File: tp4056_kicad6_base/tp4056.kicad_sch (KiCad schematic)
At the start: 32 parts, among them J1 USB_B_Micro, J10 Conn_01x02_Male, J2 Conn_01x01_Female, J3 Conn_01x01_Female, J4 Conn_01x01_Female, J5 Conn_01x01_Female, J6 Conn_01x01_Female, J7 Conn_01x01_Female, J8 Conn_01x02_Male, J9 Conn_01x02_Male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

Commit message: pcb. Board 38x18
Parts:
- J1: footprint usb_footprint:tp4056_USB_Micro-B_Molex_47346-0001_fix -> Connector_USB:USB_Micro-B_Molex-105017-0001
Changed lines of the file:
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@@
     (property "Reference" "J1" (id 0) (at 39.37 100.33 0))
     (property "Value" "USB_B_Micro" (id 1) (at 39.37 102.87 0))
-    (property "Footprint" "usb_footprint:tp4056_USB_Micro-B_Molex_47346-0001_fix" (id 2) (at 43.18 114.3 0)
+    (property "Footprint" "Connector_USB:USB_Micro-B_Molex-105017-0001" (id 2) (at 43.18 114.3 0)
       (effects (font (size 1.27 1.27)) hide)
     )
@@
     )
     (path "/ff08e3fa-c419-4101-acf6-7d150274f530"
-      (reference "J1") (unit 1) (value "USB_B_Micro") (footprint "usb_footprint:tp4056_USB_Micro-B_Molex_47346-0001_fix")
+      (reference "J1") (unit 1) (value "USB_B_Micro") (footprint "Connector_USB:USB_Micro-B_Molex-105017-0001")
     )
     (path "/f5af9e6d-b38e-432e-8453-2d6df2b3d8c9"

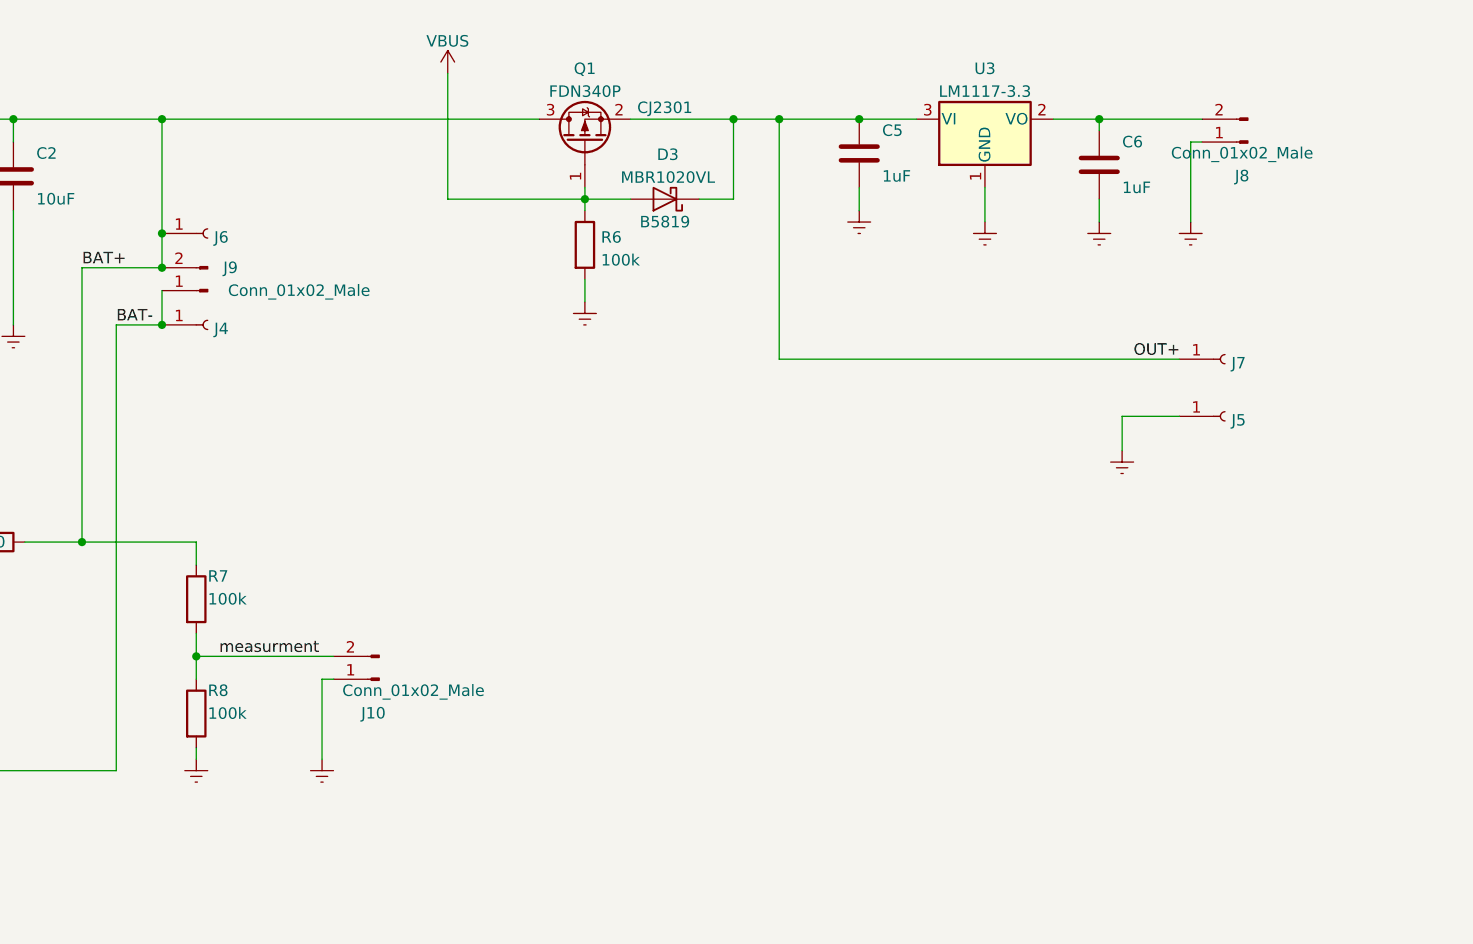
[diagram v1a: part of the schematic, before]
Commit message: sch. add voltage supervisor.
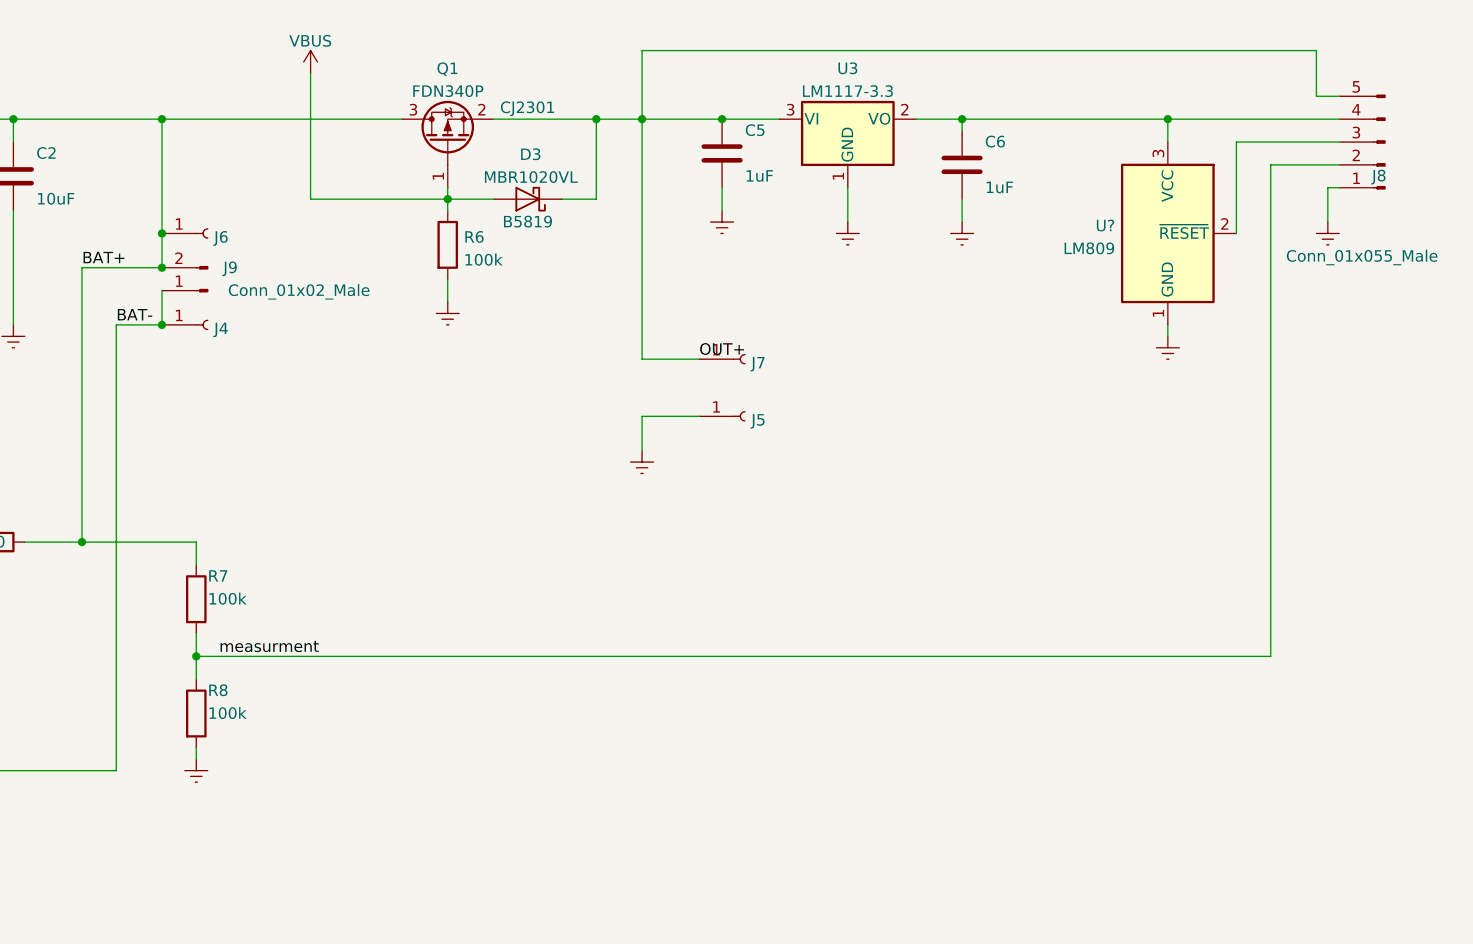
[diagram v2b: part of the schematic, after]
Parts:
- removed J10: Conn_01x02_Male, Connector_PinHeader_2.54mm:PinHeader_1x02_P2.54mm_Vertical, symbol Connector:Conn_01x02_Male
- added U?: LM809, Package_TO_SOT_SMD:SOT-23, symbol Power_Supervisor:LM809
- J8: value Conn_01x02_Male -> Conn_01x055_Male; footprint Connector_PinHeader_2.54mm:PinHeader_1x02_P2.54mm_Vertical -> Connector_PinHeader_2.54mm:PinHeader_1x04_P2.54mm_Vertical; symbol Connector:Conn_01x02_Male -> Connector:Conn_01x05_Male
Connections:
- net Earth: now also U?.1 (GND)
- net OUT+: now also J8.5 (Pin_5)
- net measurment: now also J8.2 (Pin_2)
- net at C6.1, U3.2 (VO): now also J8.4 (Pin_4), U?.3 (VCC); no longer J8.2 (Pin_2)
- new net: J8.3 (Pin_3), U?.2 (~{RESET})
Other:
- moved on the sheet: C5, C6, D3, J5, J7, Q1, R6, U3

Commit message: pcb. board 40x20 one layer
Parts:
- removed J9: Conn_01x02_Male, Connector_JST:JST_PH_B2B-PH-K_1x02_P2.00mm_Vertical, symbol Connector:Conn_01x02_Male
- C2, C4: value 10uF -> MLCC 10uF 10V 0805
- D3: footprint Diode_SMD:D_SOD-123F -> Diode_SMD_AKL:D_SOD-123F
- J8: value Conn_01x055_Male -> Conn_01x04_Male; symbol Connector:Conn_01x05_Male -> Connector:Conn_01x04_Male
- Q1: footprint Package_TO_SOT_SMD:SOT-23 -> Package_TO_SOT_SMD_AKL:SOT-23_Handsoldering
- R1, R2, R4: footprint Resistor_SMD:R_0603_1608Metric_Pad0.98x0.95mm_HandSolder -> Resistor_SMD:R_0805_2012Metric_Pad1.20x1.40mm_HandSolder
- U1: footprint Package_SO:SOIC-8-1EP_3.9x4.9mm_P1.27mm_EP2.29x3mm -> Package_SO_AKL:SOIC-8-1EP_3.9x4.9mm_P1.27mm_EP2.29x3mm
- U2: footprint Package_TO_SOT_SMD:SOT-23-6_Handsoldering -> Package_TO_SOT_SMD_AKL:SOT-23-6_Handsoldering
- U3: footprint Package_TO_SOT_SMD_AKL:SOT-23 -> Package_TO_SOT_SMD_AKL:SOT-23_Handsoldering
- U4: renamed from U?; footprint Package_TO_SOT_SMD:SOT-23 -> Package_TO_SOT_SMD_AKL:SOT-23_Handsoldering
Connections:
- net OUT+: no longer J8.5 (Pin_5)
- net at Q2.2 (D12): no longer Q2.5 (D12)
- net +3.3V: now reaches C6.1, U3.2 (VO), U4.3 (VCC)
- net +3.3V: now also J8.3 (Pin_3); no longer J8.4 (Pin_4)
- net RST: now reaches U4.2 (~{RESET})
- net RST: now also J8.4 (Pin_4); no longer J8.3 (Pin_3)
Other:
- moved on the sheet: J6

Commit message: pcb. new version 29x23. OJO Revisar disponibilidad de MOSFET!
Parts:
- C1, C2, C3, C4, C5, C6: footprint Capacitor_SMD:C_0805_2012Metric_Pad1.18x1.45mm_HandSolder -> Capacitor_SMD:C_0805_2012Metric
- Q1, U3, U4: footprint Package_TO_SOT_SMD_AKL:SOT-23_Handsoldering -> Package_TO_SOT_SMD_AKL:SOT-23
- Q2: footprint Package_TO_SOT_SMD_AKL:TSOT-23-6_HandSoldering -> Package_TO_SOT_SMD_AKL:SOT-23-6
- R1, R2, R3, R4, R5, R6, R7, R8: footprint Resistor_SMD:R_0805_2012Metric_Pad1.20x1.40mm_HandSolder -> Resistor_SMD:R_0805_2012Metric
- U2: footprint Package_TO_SOT_SMD_AKL:SOT-23-6_Handsoldering -> Package_TO_SOT_SMD_AKL:SOT-23-6
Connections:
- net +3.3V: now also J8.4 (Pin_4); no longer J8.3 (Pin_3)
- net Earth: now also J1.6 (Shield)
- net RST: now also J8.3 (Pin_3); no longer J8.4 (Pin_4)
- no-connect marks 5 -> 4
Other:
- moved on the sheet: J8

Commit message: sch. redraw and organization
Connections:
- net BAT+ renamed +BATT
- net BAT- renamed -BATT
- net OUT+ renamed VDC
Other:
- note added: "Accesorio p/ micro"
- note added: "Cargador"
- note added: "Entrada"
- note added: "Power Path"
- note added: "Protección"
- moved on the sheet: C1, C2, C3, C4, C5, C6, D1, D2, D3, J1, J2, J3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

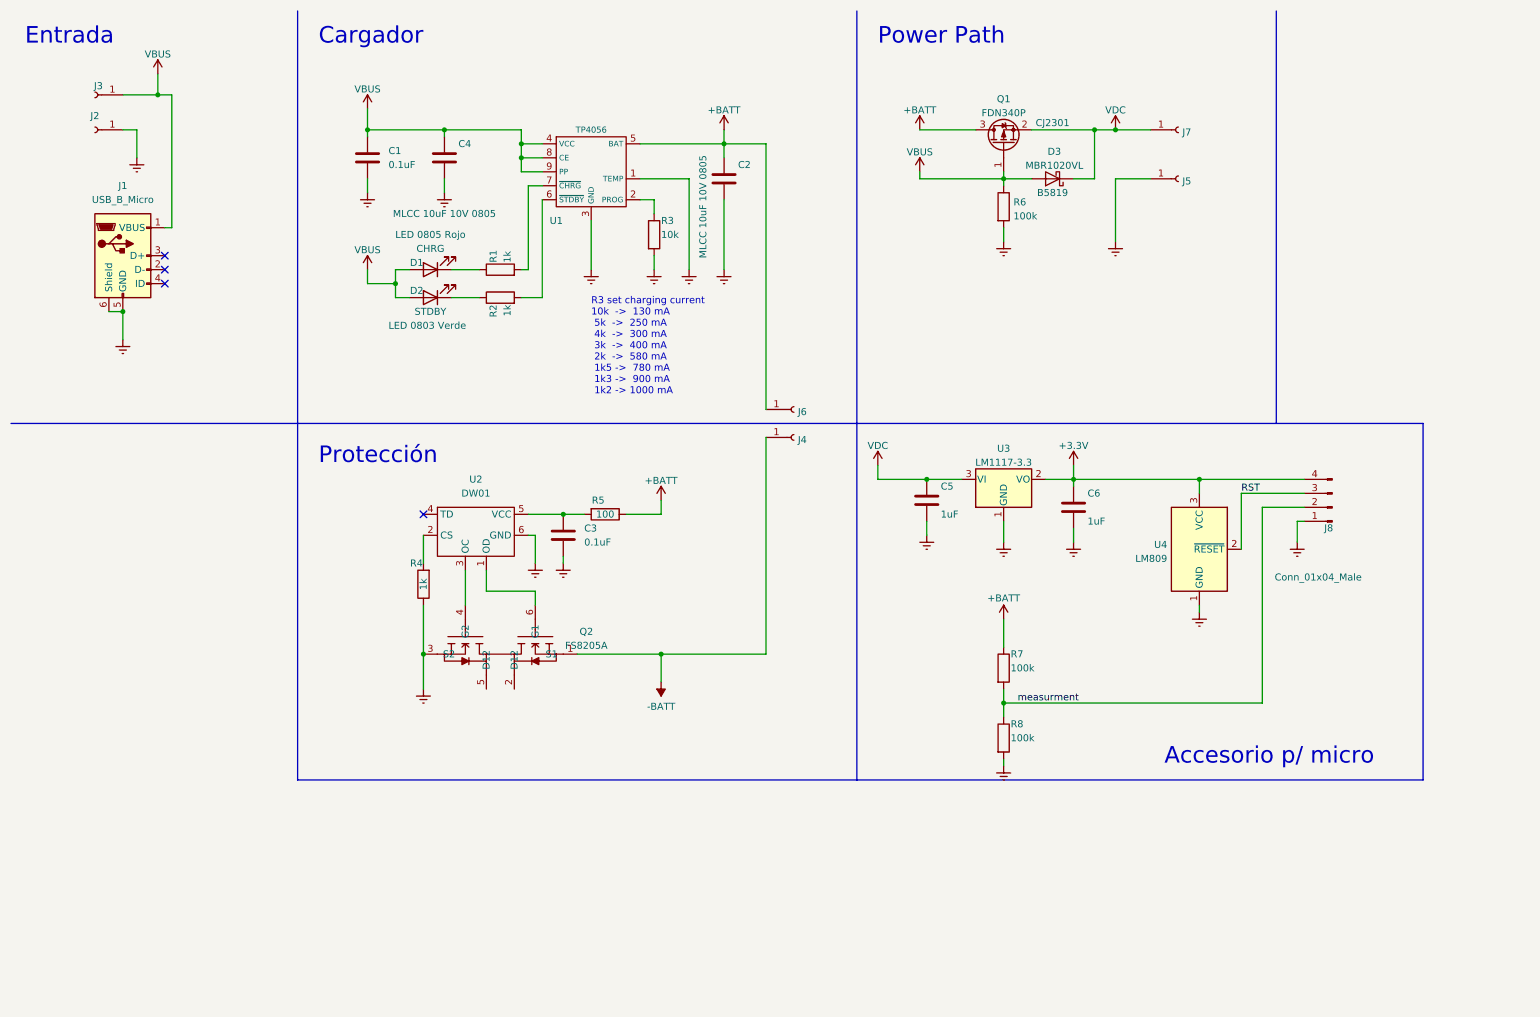
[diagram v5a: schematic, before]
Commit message: Add zero-power measurment. Some connectors change.
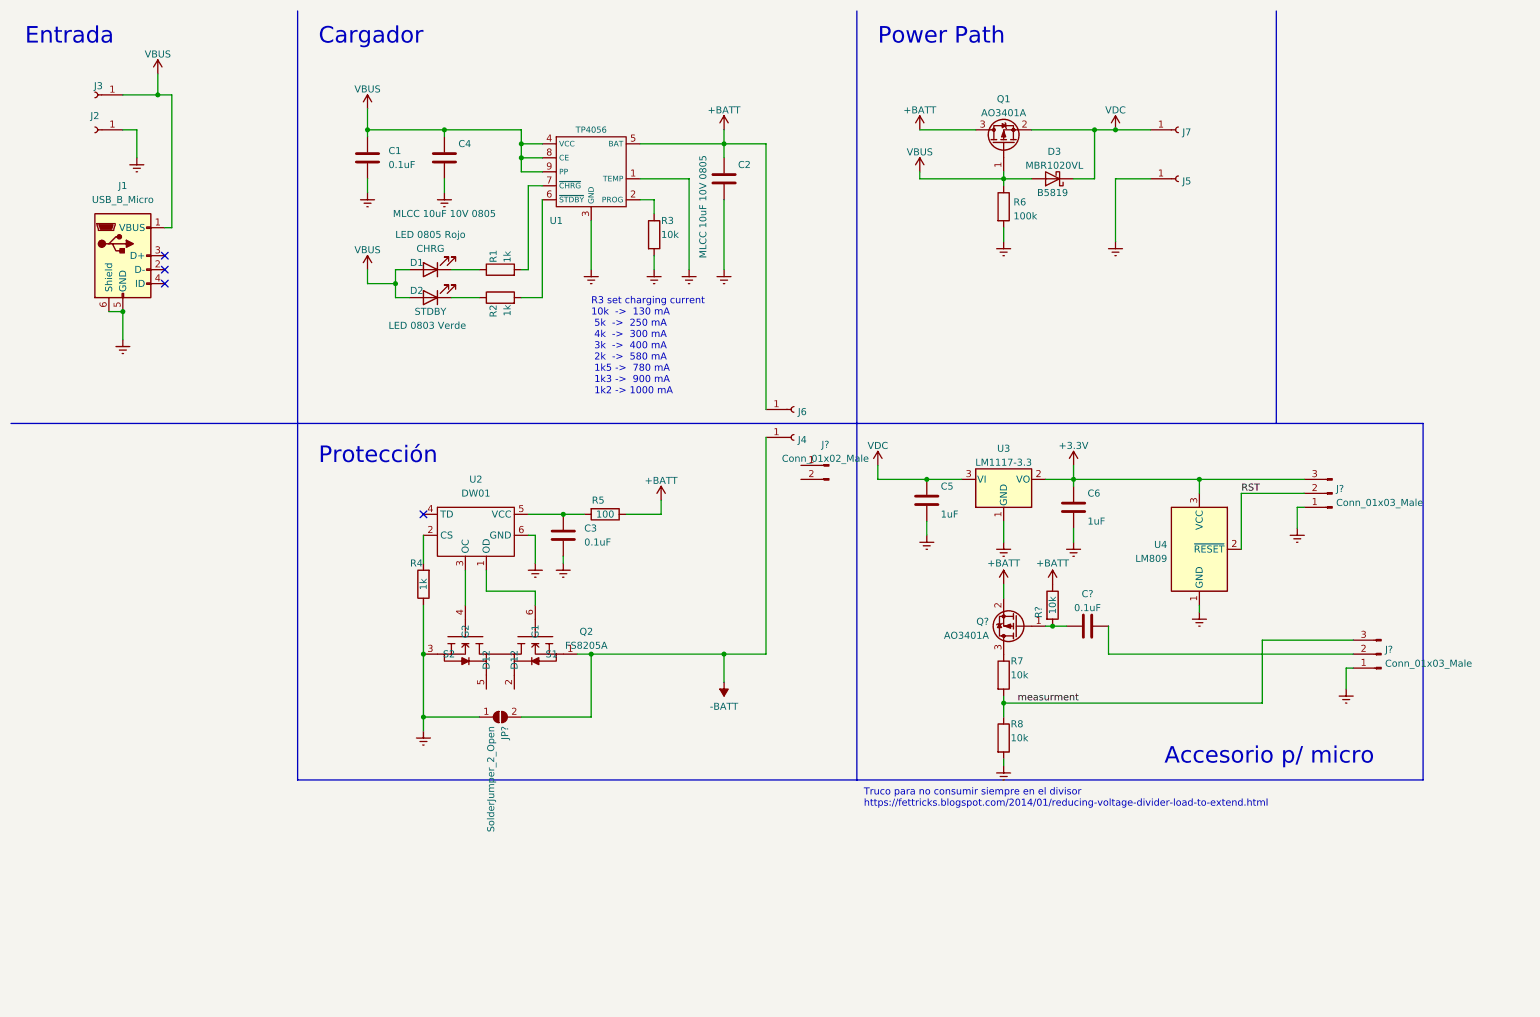
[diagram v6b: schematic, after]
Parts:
- removed J8: Conn_01x04_Male, Connector_PinHeader_2.54mm:PinHeader_1x04_P2.54mm_Vertical, symbol Connector:Conn_01x04_Male
- removed Q1: FDN340P, Package_TO_SOT_SMD_AKL:SOT-23, symbol Transistor_FET:FDN340P
- added C?: 0.1uF, Capacitor_SMD:C_0805_2012Metric, symbol Device:C
- added J?: Conn_01x02_Male, symbol Connector:Conn_01x02_Male
- added J? (x2): Conn_01x03_Male, symbol Connector:Conn_01x03_Male
- added JP?: SolderJumper_2_Open, symbol Jumper:SolderJumper_2_Open
- added Q1: AO3401A, Package_TO_SOT_SMD_AKL:SOT-23, symbol Transistor_FET:AO3401A
- added Q?: AO3401A, Package_TO_SOT_SMD:SOT-23, symbol Transistor_FET:AO3401A
- added R?: 10k, Resistor_SMD:R_0805_2012Metric, symbol Device:R
- R7, R8: value 100k -> 10k
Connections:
- net +3.3V: now also J?.3 (Pin_3)
- net +BATT: now also Q1.3 (D), Q?.2 (S), R?.1; no longer R7.1
- net -BATT: now also JP?.2 (B)
- net Earth: now also J?.1 (Pin_1), J?.1 (Pin_1), JP?.1 (A)
- net RST: now also J?.2 (Pin_2)
- net VBUS: now also Q1.1 (G)
- net VDC: now also Q1.2 (S)
- net measurment: now also J?.3 (Pin_3)
- new net: Q?.3 (D), R7.1
- new net: C?.2, J?.2 (Pin_2)
- new net: C?.1, Q?.1 (G), R?.2
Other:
- note added: "Truco para no consumir siempre en el divisor https://fettricks.blogspot.com/2014/01/reducing-voltage-divider-load-to-extend.html"
- moved on the sheet: R7

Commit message: Change conectors. Add jumpers. PCB ready 48x20.
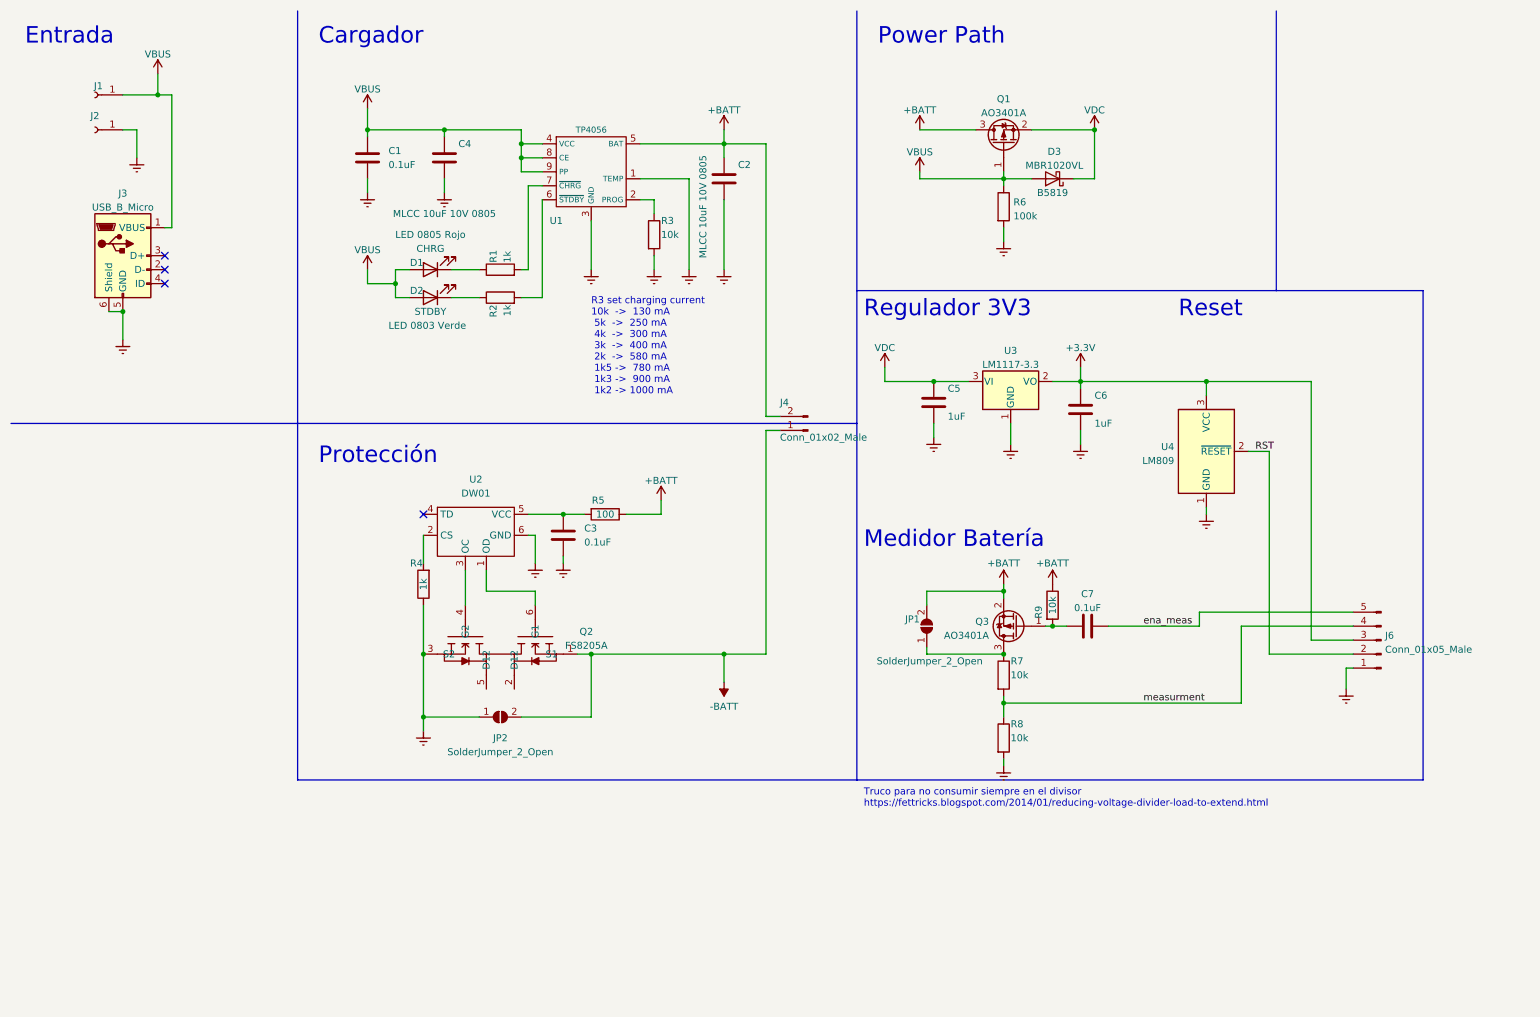
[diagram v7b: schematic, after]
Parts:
- removed J4, J5, J6, J7: Conn_01x01_Female, Connector_PinSocket_2.54mm:PinSocket_1x01_P2.54mm_Vertical, symbol Connector:Conn_01x01_Female
- removed J?: Conn_01x03_Male, symbol Connector:Conn_01x03_Male
- added JP1: SolderJumper_2_Open, Jumper:SolderJumper-2_P1.3mm_Open_TrianglePad1.0x1.5mm, symbol Jumper:SolderJumper_2_Open
- J4: renamed from J?; footprint (none) -> Connector_JST:JST_EH_B2B-EH-A_1x02_P2.50mm_Vertical
- J6: renamed from J?; value Conn_01x03_Male -> Conn_01x05_Male; footprint (none) -> Connector_JST:JST_EH_B5B-EH-A_1x05_P2.50mm_Vertical; symbol Connector:Conn_01x03_Male -> Connector:Conn_01x05_Male
- JP2: renamed from JP?; footprint (none) -> Jumper:SolderJumper-2_P1.3mm_Open_TrianglePad1.0x1.5mm
- Q3: renamed from Q?; footprint Package_TO_SOT_SMD:SOT-23 -> Package_TO_SOT_SMD_AKL:SOT-23
- gave numbers to parts that had none: 2
- renumbered J3 to J1, J1 to J3
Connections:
- net +3.3V: now also J6.3 (Pin_3)
- net +BATT: now also J4.2 (Pin_2), JP1.2 (B)
- net -BATT: now also J4.1 (Pin_1)
- net RST: now also J6.2 (Pin_2)
- net measurment: now also J6.4 (Pin_4); no longer J6.3 (Pin_3)
- net at Q3.3 (D), R7.1: now also JP1.1 (A)
- net ena_meas: now reaches C7.2
- net ena_meas: now also J6.5 (Pin_5); no longer J6.2 (Pin_2)
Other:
- note added: "Medidor Batería"
- note added: "Regulador 3V3"
- note added: "Reset"
- note removed: "Accesorio p/ micro"
- moved on the sheet: C5, C6, J4, U3, U4
